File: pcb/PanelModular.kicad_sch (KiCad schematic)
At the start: 45 parts, among them J1 KEY_1, J1.1 Conn_01x08, J10 KEY_10, J11 LED_1, J12 LED_2, J13 LED_3, J14 LED_4, J15 LED_5, J16 LED_6, J17 LED_7, J18 LED_8, J19 ADC_1, J2 KEY_2, J2.1 Conn_01x08, J20 ADC_2, J21 ADC_3, J22 E_STOP, J23 ENCODER, J24 START, J25 STOP, J26 E_STOP_LED, J27 WS2811, J28 MIST, J29 KEY_11, J3 KEY_3, J30 KEY_12, J31 BREAK, J4 KEY_4, J5 KEY_5, J6 KEY_6, J7 KEY_7, J8 KEY_8, J9 KEY_9, U1 LM7805_TO220, U2 Pico, U4 74LVC1G17

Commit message: I2C ready version
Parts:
- added J32: I2C_3V3, Connector_JST:JST_XH_B4B-XH-A_1x04_P2.50mm_Vertical, symbol Connector:Conn_01x04_Pin
- added J33: I2C_5V, Connector_JST:JST_XH_B4B-XH-A_1x04_P2.50mm_Vertical, symbol Connector:Conn_01x04_Pin
- added JP1: LED_Power_Jumper, Jumper:SolderJumper-3_P1.3mm_Bridged12_Pad1.0x1.5mm_NumberLabels, symbol Jumper:SolderJumper_3_Bridged12
- added JP2: I2C_Power Jumper, Jumper:SolderJumper-3_P1.3mm_Bridged12_Pad1.0x1.5mm_NumberLabels, symbol Jumper:SolderJumper_3_Bridged12
- added JP3: OverrideU4, Jumper:SolderJumper-2_P1.3mm_Open_Pad1.0x1.5mm, symbol Jumper:SolderJumper_2_Open
- added JP4: Enable U4, Jumper:SolderJumper-2_P1.3mm_Bridged_Pad1.0x1.5mm, symbol Jumper:SolderJumper_2_Bridged
- added Q1, Q2: BSS138, Package_TO_SOT_SMD:SOT-23, symbol Transistor_FET:BSS138
- added R2, R3, R4, R5: 10K, Resistor_SMD:R_0805_2012Metric_Pad1.20x1.40mm_HandSolder, symbol Device:R
- added U3: PCF8574, Package_SO:SO-16_5.3x10.2mm_P1.27mm, symbol Interface_Expansion:PCF8574
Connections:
- net +12V: now also JP1.3 (B); no longer J28.3 (Pin_3)
- net +24V: now also JP1.1 (A); no longer D1.14 (V), D2.14 (V), J11.2 (Pin_2), J12.2 (Pin_2), J13.2 (Pin_2), J14.2 (Pin_2), J15.2 (Pin_2), J16.2 (Pin_2), J17.2 (Pin_2), J18.2 (Pin_2)
- net +3.3V: now also JP2.1 (A), Q1.1 (G), Q2.1 (G), R3.2, R4.2, U3.16 (VDD)
- net +5V: now also J28.3 (Pin_3), J33.4 (Pin_4), JP2.3 (B), R2.2, R5.2
- net GND: now also J32.1 (Pin_1), J33.1 (Pin_1), U3.1 (A0), U3.2 (A1), U3.3 (A2), U3.8 (VSS)
- net LED_1: now also U3.4 (P0); no longer U2.24 (GPIO18)
- net LED_2: now also U3.5 (P1); no longer U2.25 (GPIO19)
- net LED_3: now also U3.6 (P2); no longer U2.26 (GPIO20)
- net LED_4: now also U3.7 (P3); no longer U2.27 (GPIO21)
- net LED_5: now also U3.9 (P4); no longer U2.22 (GPIO17)
- net LED_6: now also U3.10 (P5); no longer U2.21 (GPIO16)
- net LED_7: now also U3.11 (P6); no longer U2.20 (GPIO15)
- net LED_8: now also U3.12 (P7); no longer U2.19 (GPIO14)
- net WS_DATA: now also U2.27 (GPIO21), JP3.1 (A); no longer U2.16 (GPIO12)
- net at R1.1: now also JP3.2 (B), JP4.2 (B); no longer U4.4
- net SCL: now reaches U2.17 (GPIO13)
- net SCL: now also J32.3 (Pin_3), U3.15 (SDA)
- net MIST_AIR_3V3 renamed MIST_AIR
- net MIST_VALVE_3V3 renamed MIST_VALVE
- net REMOTE_EN_3V3 renamed REMOTE_EN
- new net: J32.4 (Pin_4), JP2.2 (C)
- new net: JP4.1 (A), U4.4
- new net +U_LED: D1.14 (V), D2.14 (V), J11.2 (Pin_2), J12.2 (Pin_2), J13.2 (Pin_2), J14.2 (Pin_2), J15.2 (Pin_2), J16.2 (Pin_2), J17.2 (Pin_2), J18.2 (Pin_2), JP1.2 (C)
- new net SCL2: Q1.2 (S), R3.1, U2.20 (GPIO15)
- new net SCL_5V: J33.3 (Pin_3), Q1.3 (D), R2.1
- new net SDA: J32.2 (Pin_2), U2.16 (GPIO12), U3.14 (SCL)
- new net SDA2: Q2.2 (S), R4.1, U2.19 (GPIO14)
- new net SDA_5V: J33.2 (Pin_2), Q2.3 (D), R5.1
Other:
- moved on the sheet: J1, J10, J2, J22, J23, J24, J25, J26, J28, J29, J3, J30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

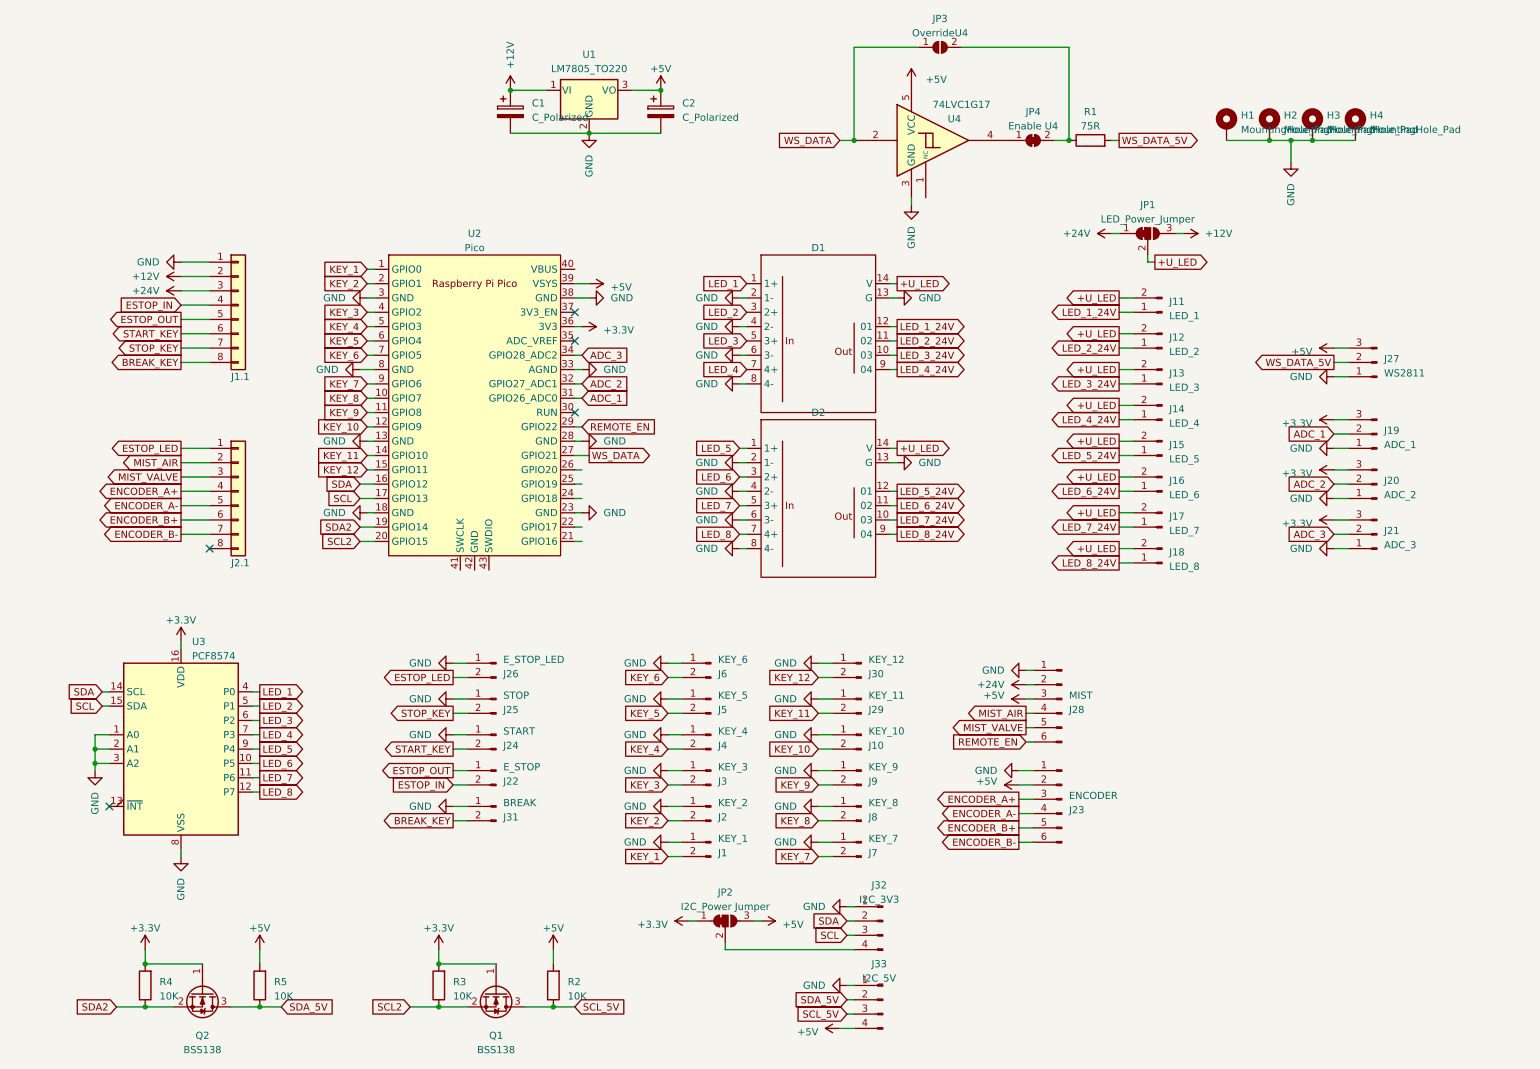
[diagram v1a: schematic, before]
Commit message: The first ordered Version, missing i2c pullups and wrong i2c connected to external
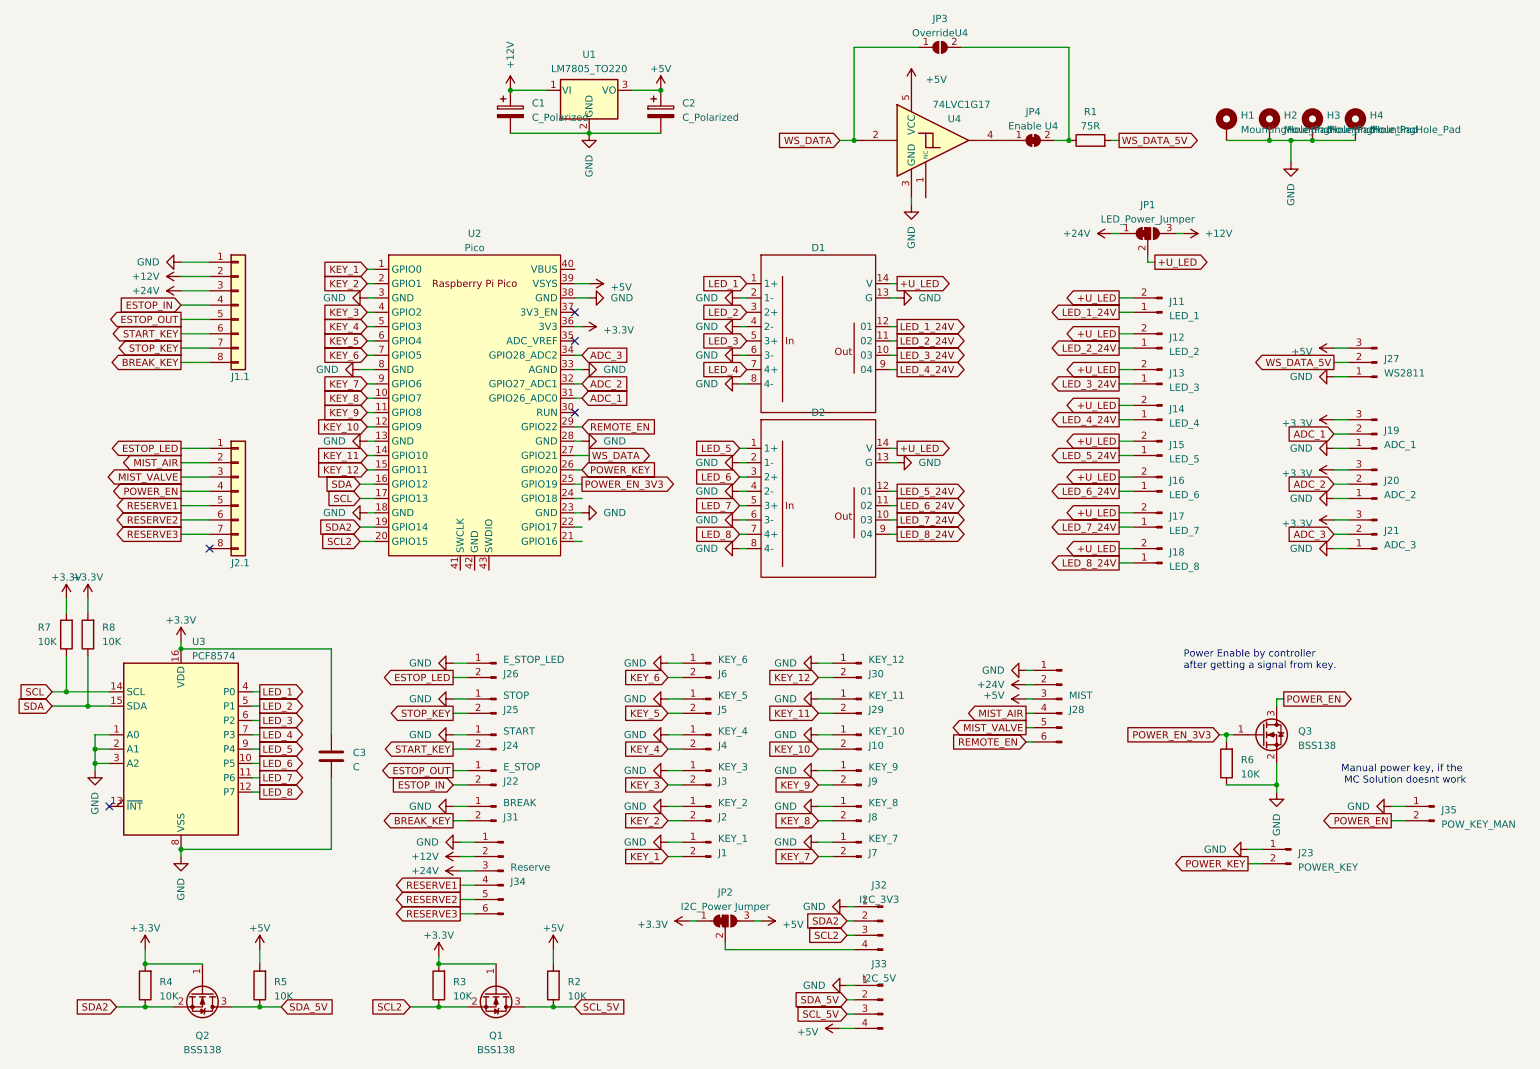
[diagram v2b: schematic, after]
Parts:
- removed J23: ENCODER, Connector_JST:JST_XH_B6B-XH-A_1x06_P2.50mm_Vertical, symbol Connector:Conn_01x06_Pin
- added C3: C, Capacitor_SMD:C_0805_2012Metric_Pad1.18x1.45mm_HandSolder, symbol Device:C
- added J23: POWER_KEY, Connector_JST:JST_XH_B2B-XH-A_1x02_P2.50mm_Vertical, symbol Connector:Conn_01x02_Pin
- added J34: Reserve, Connector_JST:JST_XH_B6B-XH-A_1x06_P2.50mm_Vertical, symbol Connector:Conn_01x06_Pin
- added J35: POW_KEY_MAN, Connector_JST:JST_XH_B2B-XH-A_1x02_P2.50mm_Vertical, symbol Connector:Conn_01x02_Pin
- added Q3: BSS138, Package_TO_SOT_SMD:SOT-23_Handsoldering, symbol Transistor_FET:BSS138
- added R6, R7, R8: 10K, Resistor_SMD:R_0805_2012Metric_Pad1.20x1.40mm_HandSolder, symbol Device:R
- Q1, Q2: footprint Package_TO_SOT_SMD:SOT-23 -> Package_TO_SOT_SMD:SOT-23_Handsoldering
- U3: footprint Package_SO:SO-16_5.3x10.2mm_P1.27mm -> Library:SO-16_7,7x10.2mm_P1.27mm-PCF8574
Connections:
- net +12V: now also J34.2 (Pin_2)
- net +24V: now also J34.3 (Pin_3)
- net +3.3V: now also C3.1, R7.2, R8.2
- net GND: now also C3.2, J23.1 (Pin_1), J34.1 (Pin_1), J35.1 (Pin_1), Q3.2 (S), R6.1
- net SCL: now also U3.14 (SCL), R7.1; no longer J32.3 (Pin_3), U3.15 (SDA)
- net SCL2: now also J32.3 (Pin_3)
- net SDA: now also U3.15 (SDA), R8.1; no longer J32.2 (Pin_2), U3.14 (SCL)
- net SDA2: now also J32.2 (Pin_2)
- net POWER_EN_3V3: now reaches U2.25 (GPIO19)
- net POWER_EN_3V3: now also Q3.1 (G), R6.2
- net POWER_KEY: now reaches U2.26 (GPIO20)
- net POWER_KEY: now also J23.2 (Pin_2)
- net ENCODER_A+ renamed POWER_EN
- net POWER_EN: now also J35.2 (Pin_2), Q3.3 (D)
- net ENCODER_A- renamed RESERVE1
- net RESERVE1: now also J34.4 (Pin_4)
- net ENCODER_B+ renamed RESERVE2
- net RESERVE2: now also J34.5 (Pin_5)
- net ENCODER_B- renamed RESERVE3
- net RESERVE3: now also J34.6 (Pin_6)
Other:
- note added: "Manual power key, if the MC Solution doesnt work"
- note added: "Power Enable by controller after getting a signal from key."

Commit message: Revert "The first ordered Version, missing i2c pullups and wrong i2c connected to external"
This reverts commit 4b4ee199a77fa0146eabba4f0e18928ce2f89e34.
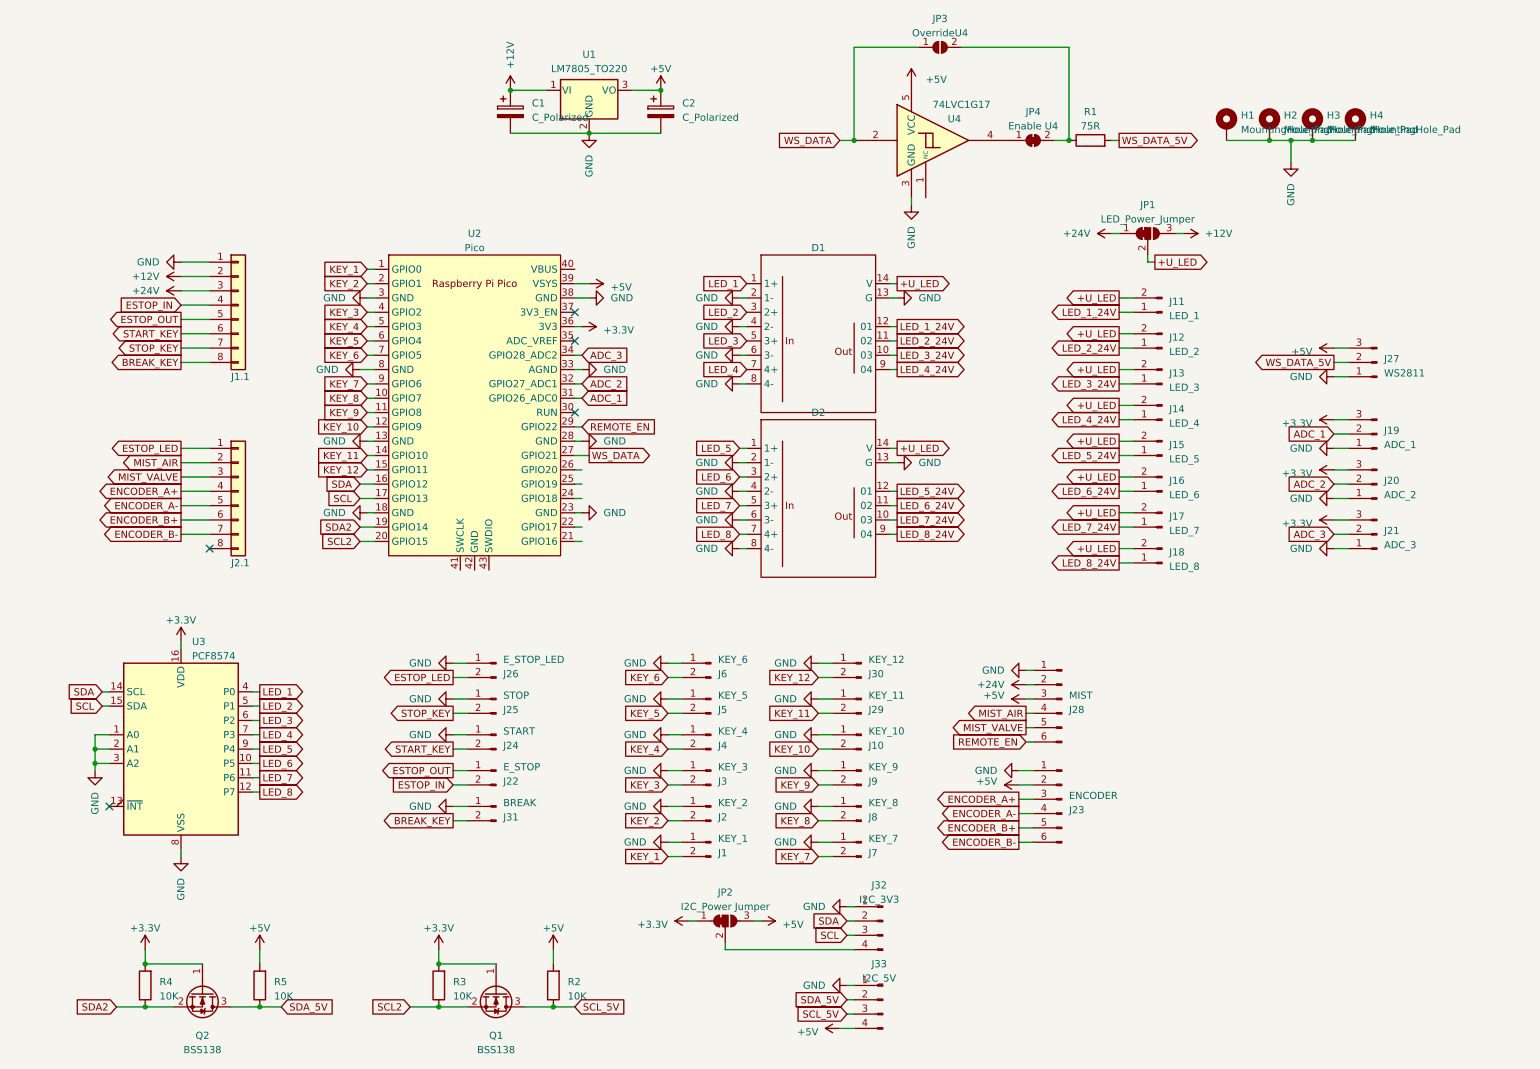
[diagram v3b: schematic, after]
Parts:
- removed C3: C, Capacitor_SMD:C_0805_2012Metric_Pad1.18x1.45mm_HandSolder, symbol Device:C
- removed J23: POWER_KEY, Connector_JST:JST_XH_B2B-XH-A_1x02_P2.50mm_Vertical, symbol Connector:Conn_01x02_Pin
- removed J34: Reserve, Connector_JST:JST_XH_B6B-XH-A_1x06_P2.50mm_Vertical, symbol Connector:Conn_01x06_Pin
- removed J35: POW_KEY_MAN, Connector_JST:JST_XH_B2B-XH-A_1x02_P2.50mm_Vertical, symbol Connector:Conn_01x02_Pin
- removed Q3: BSS138, Package_TO_SOT_SMD:SOT-23_Handsoldering, symbol Transistor_FET:BSS138
- removed R6, R7, R8: 10K, Resistor_SMD:R_0805_2012Metric_Pad1.20x1.40mm_HandSolder, symbol Device:R
- added J23: ENCODER, Connector_JST:JST_XH_B6B-XH-A_1x06_P2.50mm_Vertical, symbol Connector:Conn_01x06_Pin
- Q1, Q2: footprint Package_TO_SOT_SMD:SOT-23_Handsoldering -> Package_TO_SOT_SMD:SOT-23
- U3: footprint Library:SO-16_7,7x10.2mm_P1.27mm-PCF8574 -> Package_SO:SO-16_5.3x10.2mm_P1.27mm
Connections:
- net +5V: now also J23.2 (Pin_2)
- net GND: now also J23.1 (Pin_1)
- net SCL: now also J32.3 (Pin_3), U3.15 (SDA); no longer U3.14 (SCL)
- net SCL2: no longer J32.3 (Pin_3)
- net SDA: now also J32.2 (Pin_2), U3.14 (SCL); no longer U3.15 (SDA)
- net SDA2: no longer J32.2 (Pin_2)
- net POWER_EN renamed ENCODER_A+
- net ENCODER_A+: now also J23.3 (Pin_3)
- net POWER_EN_3V3: no longer names the net of U2.25 (GPIO19)
- net POWER_KEY: no longer names the net of U2.26 (GPIO20)
- net RESERVE1 renamed ENCODER_A-
- net ENCODER_A-: now also J23.4 (Pin_4)
- net RESERVE2 renamed ENCODER_B+
- net ENCODER_B+: now also J23.5 (Pin_5)
- net RESERVE3 renamed ENCODER_B-
- net ENCODER_B-: now also J23.6 (Pin_6)
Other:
- note removed: "Manual power key, if the MC Solution doesnt work"
- note removed: "Power Enable by controller after getting a signal from key."

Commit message: Really the first ordered Version, missing i2c pullups and wrong i2c connected to external
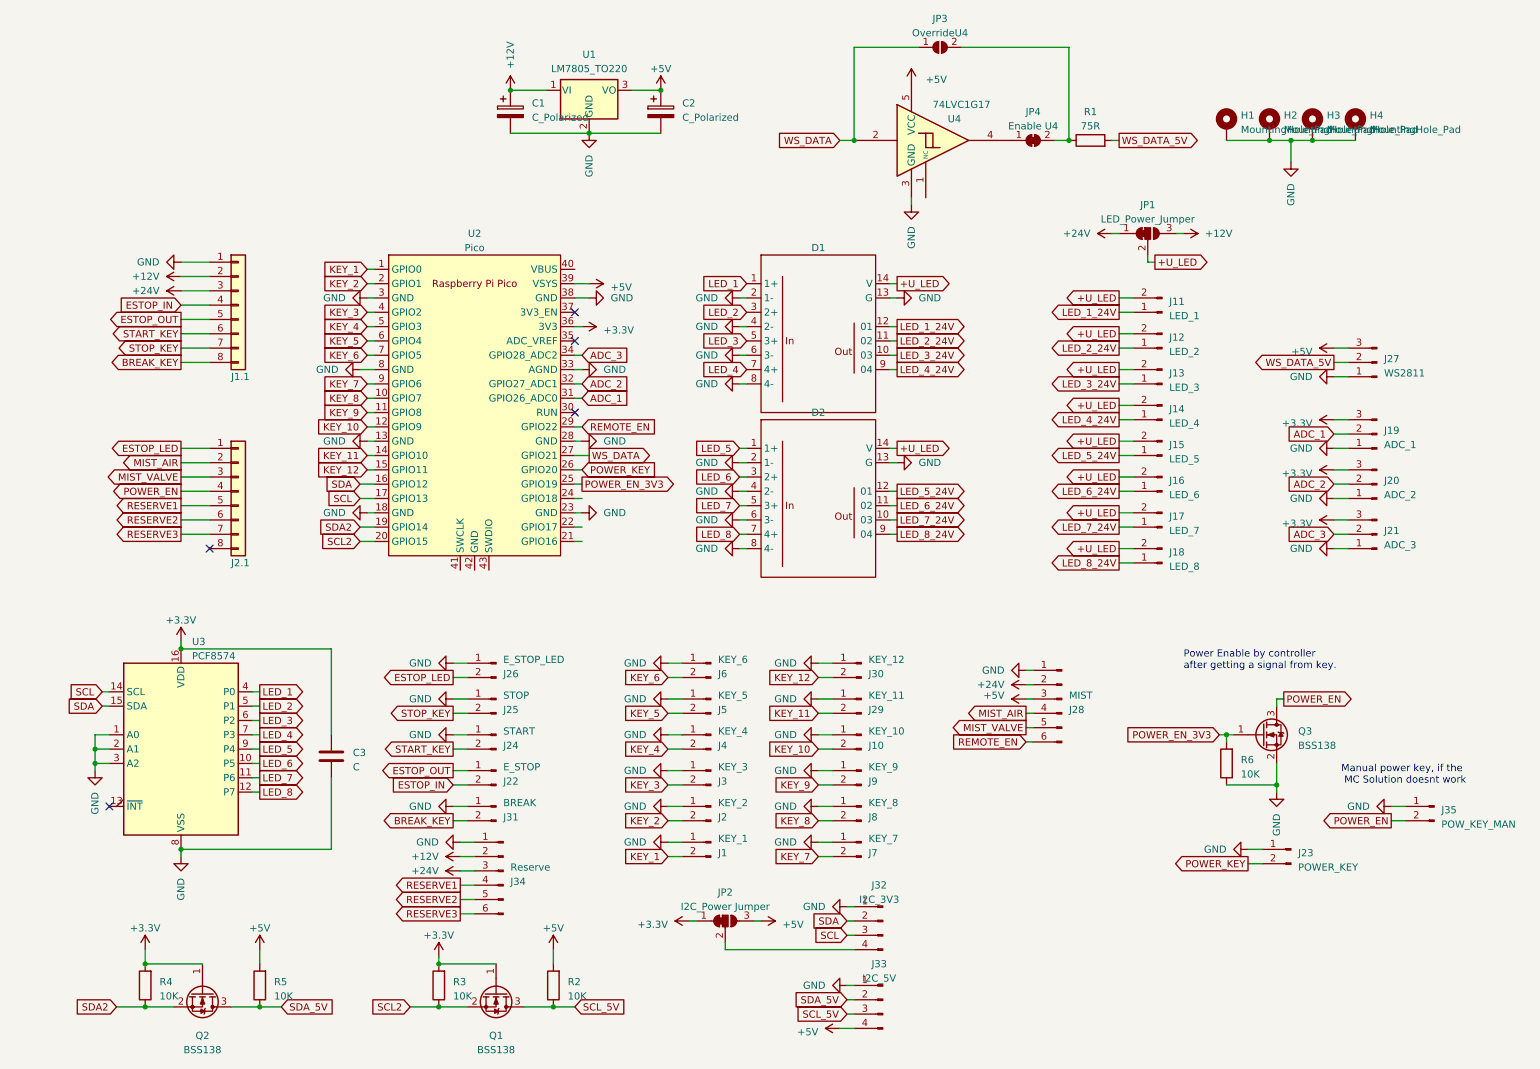
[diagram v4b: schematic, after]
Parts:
- removed J23: ENCODER, Connector_JST:JST_XH_B6B-XH-A_1x06_P2.50mm_Vertical, symbol Connector:Conn_01x06_Pin
- added C3: C, Capacitor_SMD:C_0805_2012Metric_Pad1.18x1.45mm_HandSolder, symbol Device:C
- added J23: POWER_KEY, Connector_JST:JST_XH_B2B-XH-A_1x02_P2.50mm_Vertical, symbol Connector:Conn_01x02_Pin
- added J34: Reserve, Connector_JST:JST_XH_B6B-XH-A_1x06_P2.50mm_Vertical, symbol Connector:Conn_01x06_Pin
- added J35: POW_KEY_MAN, Connector_JST:JST_XH_B2B-XH-A_1x02_P2.50mm_Vertical, symbol Connector:Conn_01x02_Pin
- added Q3: BSS138, Package_TO_SOT_SMD:SOT-23_Handsoldering, symbol Transistor_FET:BSS138
- added R6: 10K, Resistor_SMD:R_0805_2012Metric_Pad1.20x1.40mm_HandSolder, symbol Device:R
- Q1, Q2: footprint Package_TO_SOT_SMD:SOT-23 -> Package_TO_SOT_SMD:SOT-23_Handsoldering
- U3: footprint Package_SO:SO-16_5.3x10.2mm_P1.27mm -> Library:SO-16_7,7x10.2mm_P1.27mm-PCF8574
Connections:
- net +12V: now also J34.2 (Pin_2)
- net +24V: now also J34.3 (Pin_3)
- net +3.3V: now also C3.1
- net GND: now also C3.2, J23.1 (Pin_1), J34.1 (Pin_1), J35.1 (Pin_1), Q3.2 (S), R6.1
- net SCL: now also U3.14 (SCL); no longer U3.15 (SDA)
- net SDA: now also U3.15 (SDA); no longer U3.14 (SCL)
- net POWER_EN_3V3: now reaches U2.25 (GPIO19)
- net POWER_EN_3V3: now also Q3.1 (G), R6.2
- net POWER_KEY: now reaches U2.26 (GPIO20)
- net POWER_KEY: now also J23.2 (Pin_2)
- net ENCODER_A+ renamed POWER_EN
- net POWER_EN: now also J35.2 (Pin_2), Q3.3 (D)
- net ENCODER_A- renamed RESERVE1
- net RESERVE1: now also J34.4 (Pin_4)
- net ENCODER_B+ renamed RESERVE2
- net RESERVE2: now also J34.5 (Pin_5)
- net ENCODER_B- renamed RESERVE3
- net RESERVE3: now also J34.6 (Pin_6)
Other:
- note added: "Manual power key, if the MC Solution doesnt work"
- note added: "Power Enable by controller after getting a signal from key."
